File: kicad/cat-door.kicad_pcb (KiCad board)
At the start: 2 copper layers, 25 x 48.6 mm, 18 parts, among them U1 ATtiny84-20PU, U2 L293D, U3 LF50_TO220

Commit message: PCB seems done
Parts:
- removed JPOWER1: Conn_01x02, Connector_PinSocket_2.54mm:PinSocket_1x02_P2.54mm_Vertical
- removed R3: 10k, Resistor_THT:R_Axial_DIN0207_L6.3mm_D2.5mm_P10.16mm_Horizontal
- added G***: LOGO, Cat Door:cat, B.Cu at (85.2, 39.8)
- added J1: Barrel_Jack_Switch, Cat Door:CUI_PJ-044AH, F.Cu at (71.5, 41.9)
- C1, C2, D1, D2, D3, D4, JPENCIL1, R1, R2, R4, R5, U1, U2, U3: moved to B.Cu
- moved R1 37.0 mm to (76.4, 72.4), turned to 180 degrees
- moved U2 36.3 mm to (78.9, 76.0)
- moved D1 32.5 mm to (68.9, 77.1), turned to 0 degrees
- moved R4 31.2 mm to (85.0, 55.4), turned to 90 degrees
- moved D3 28.4 mm to (68.9, 75.0), turned to 0 degrees
- moved R5 27.9 mm to (82.0, 55.4)
- moved U3 24.4 mm to (78.9, 37.6)
- moved JPENCIL1 23.9 mm to (72.7, 61.6), turned to 270 degrees
- moved D4 23.7 mm to (68.9, 66.9), turned to 0 degrees
- moved C2 20.9 mm to (65.2, 39.7), turned to 90 degrees
- moved U1 20.0 mm to (63.6, 47.0), turned to 270 degrees
- moved R2 19.4 mm to (63.7, 67.4)
- moved D2 13.9 mm to (68.9, 64.6), turned to 0 degrees
- moved C1 13.1 mm to (63.1, 44.3), turned to 0 degrees
- moved JCTRL1 7.39 mm to (67.7, 58.1), turned to 90 degrees
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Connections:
- JCTRL1 pad 1: /sw_closed_i -> /sw_open_i
- JCTRL1 pad 2: /sw_open_i -> /sw_closed_i
- JOUTER1 pad 1: /sens_open_i -> Net-(JOUTER1-Pad1)
- JOUTER1 pad 2: /sens_closed_i -> Net-(JOUTER1-Pad2)
- JOUTER1 pad 4: Net-(JOUTER1-Pad4) -> /sens_closed_i
- JOUTER1 pad 5: Net-(JOUTER1-Pad5) -> /sens_open_i
- R4 pad 1: /sw_closed_i -> /sw_open_i
- R5 pad 1: /sw_open_i -> /sw_closed_i
- U1 pad 4: Net-(R3-Pad2) -> +5V
- U2 pad 11: Net-(JOUTER1-Pad4) -> Net-(JOUTER1-Pad1)
- U2 pad 14: Net-(JOUTER1-Pad5) -> Net-(JOUTER1-Pad2)
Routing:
- net +5V: track 54.5 -> 100.6 mm
- net +9V: track 67.8 -> 29.6 mm
- net /sens_open_i: track 27.8 -> 55.5 mm
- net /sens_closed_i: track 21.2 -> 46.3 mm
- net Net-(JOUTER1-Pad1): track 0.00 -> 24.7 mm
- net Net-(JOUTER1-Pad4): track 19.4 -> 0.00 mm
- net Net-(JOUTER1-Pad2): track 0.00 -> 19.1 mm
- net GND: track 92.9 -> 111.8 mm
- net Net-(JOUTER1-Pad5): track 14.9 -> 0.00 mm
- net Net-(JPENCIL1-Pad2): track 19.1 -> 4.39 mm
- net /sw_closed_i: track 25.8 -> 13.5 mm
- net /outer_down_o: track 33.6 -> 45.3 mm
- net /flshgnd: track 21.5 -> 11.7 mm
- net Net-(JPENCIL1-Pad1): track 21.2 -> 12.4 mm
- net /inner_up_o: track 29.3 -> 36.0 mm
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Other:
- board size 25 x 48.6 mm -> 28.9 x 43.1 mm
- board text added: "Mark's Cat Door Rev. 2"

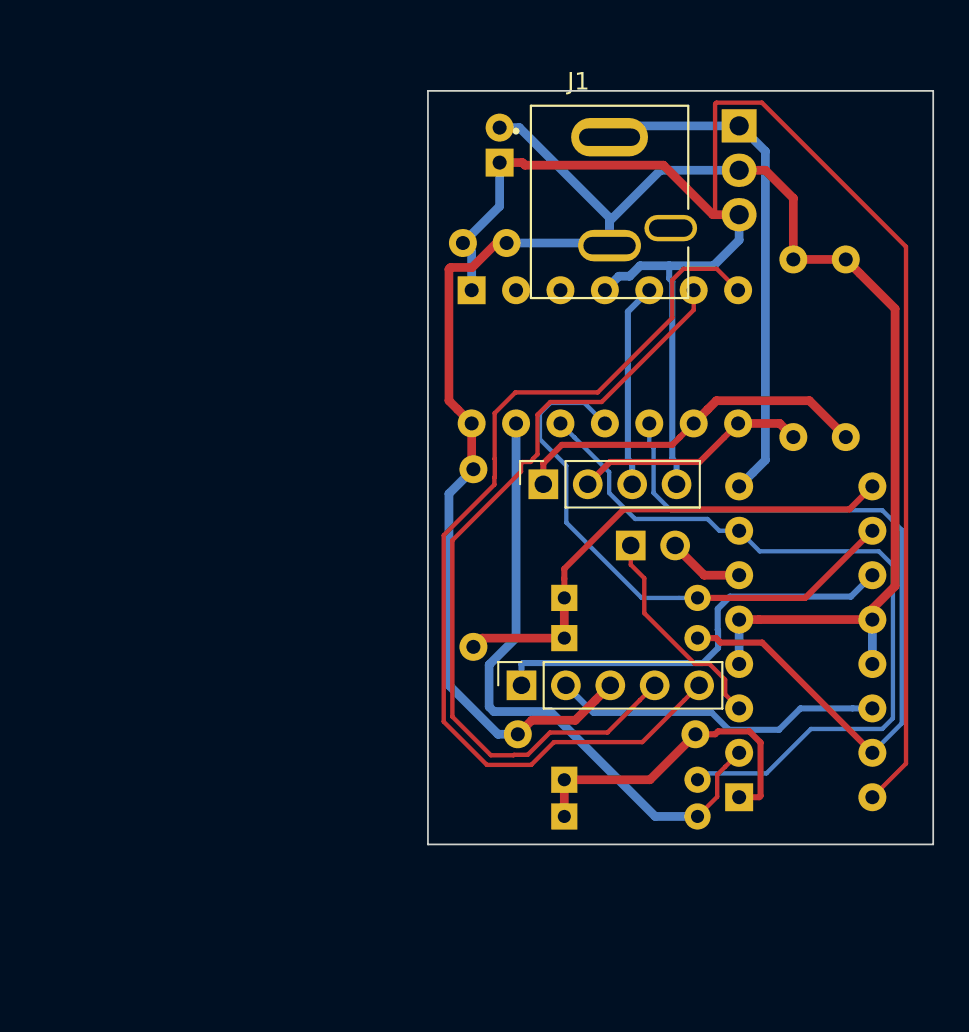
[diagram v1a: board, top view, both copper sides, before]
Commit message: the measurements on the PCb were all wrong. Until now!
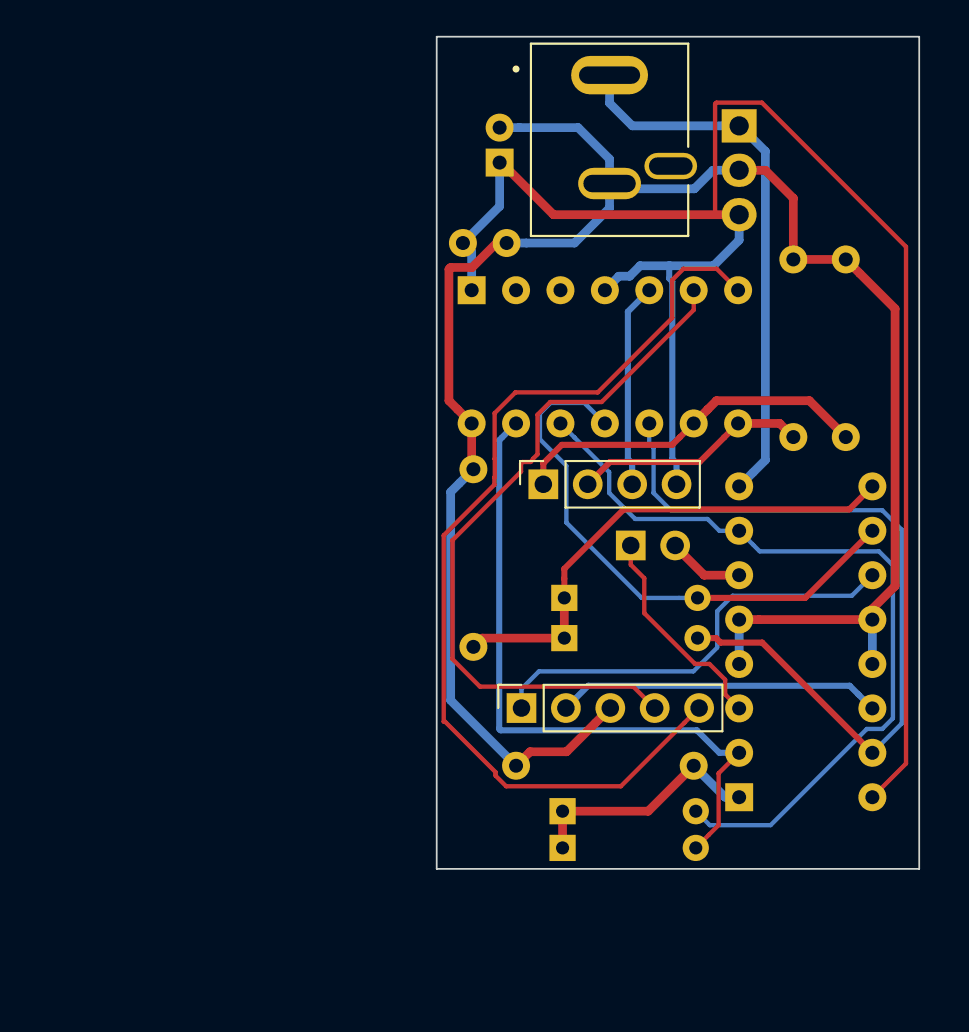
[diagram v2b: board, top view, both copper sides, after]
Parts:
- moved J1 3.55 mm to (71.5, 38.4)
- moved G*** 2.65 mm to (84.7, 37.2)
- moved D1 1.80 mm to (68.8, 78.9)
- moved D3 1.80 mm to (68.8, 76.8)
- moved R1 1.80 mm to (76.3, 74.2)
- moved JOUTER1 1.30 mm to (66.5, 70.9)
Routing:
- net Net-(D1-Pad1): track 19.0 -> 14.0 mm
- net /sens_closed_i: track 46.3 -> 41.5 mm
- net /inner_up_o: track 36.0 -> 38.6 mm
- net +9V: track 29.6 -> 31.4 mm
- net /inner_down_o: track 44.5 -> 46.0 mm
- net /sens_open_i: track 55.5 -> 56.1 mm
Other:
- board size 28.9 x 43.1 mm -> 27.6 x 47.6 mm

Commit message: horizontal and vertical traces separated.
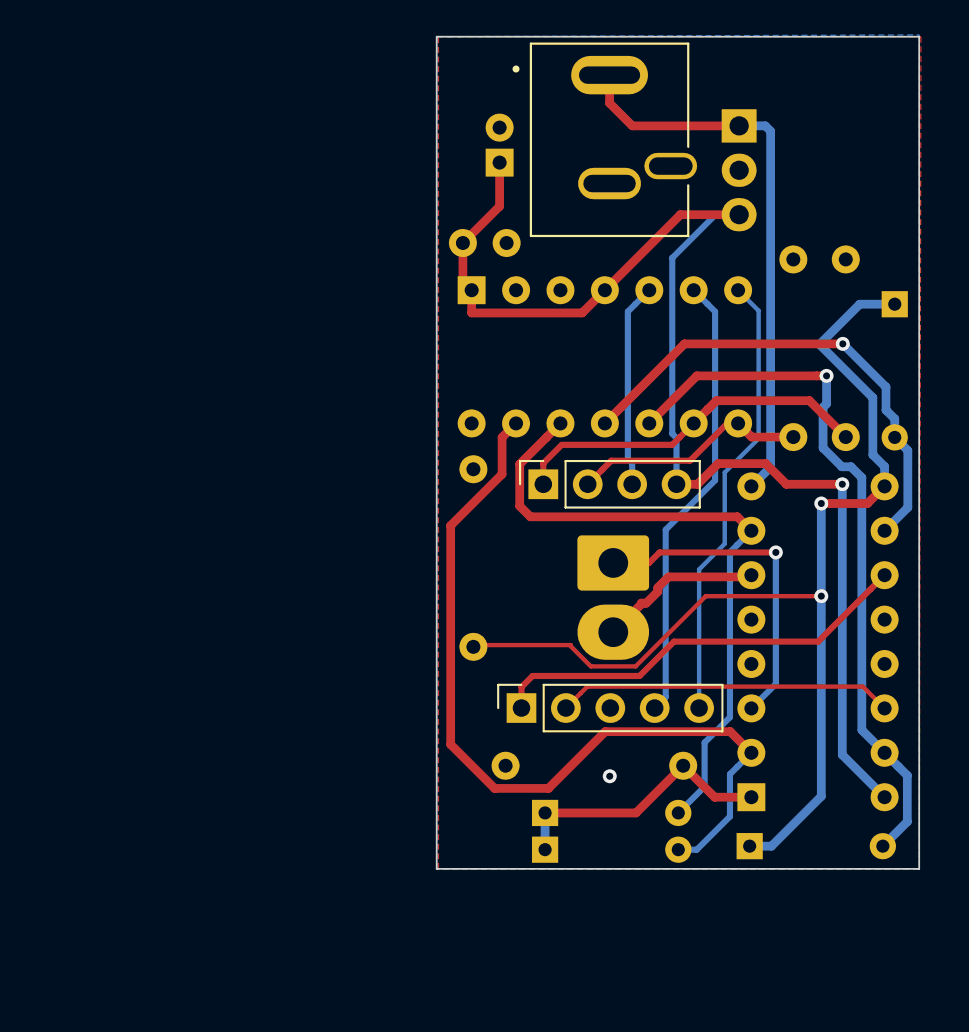
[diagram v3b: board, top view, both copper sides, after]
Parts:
- JPENCIL1: footprint Connector_PinSocket_2.54mm:PinSocket_1x02_P2.54mm_Vertical -> Connector_Molex:Molex_KK-396_A-41791-0002_1x02_P3.96mm_Vertical
- moved D2 25.3 mm to (87.8, 47.8), turned to 270 degrees
- moved D4 15.9 mm to (79.5, 78.8)
- moved JPENCIL1 1.41 mm to (71.7, 62.6)
- moved D3 1.00 mm to (67.8, 76.9)
- moved D1 1.00 mm to (67.8, 79.0)
- moved U2 0.70 mm to (79.6, 76.0)
- moved R1 0.60 mm to (75.7, 74.2)
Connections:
- U1 pad 2: Net-(U1-Pad2) -> GND
- U1 pad 3: Net-(U1-Pad3) -> GND
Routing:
- net GND: track 111.7 -> 0.00 mm, vias 0 -> 1
- net Net-(D2-Pad1): track 28.9 -> 63.1 mm, vias 0 -> 2
- net /sens_open_i: track 56.1 -> 25.8 mm
- net +5V: track 100.6 -> 74.6 mm, vias 0 -> 1
- net /sens_closed_i: track 41.5 -> 25.8 mm
- net /inner_up_o: track 38.6 -> 47.9 mm
- net /inner_down_o: track 46.0 -> 37.4 mm
- net Net-(JPENCIL1-Pad1): track 12.4 -> 19.0 mm, vias 0 -> 1
- net Net-(JPENCIL1-Pad2): track 4.39 -> 9.42 mm
- net /outer_down_o: track 45.3 -> 41.1 mm, vias 0 -> 1
- net /outer_up_o: track 32.2 -> 28.3 mm, vias 0 -> 1
- net Net-(D1-Pad1): track 14.0 -> 15.8 mm
- net +9V: track 31.4 -> 32.3 mm
- net Net-(JOUTER1-Pad2): track 18.6 -> 19.3 mm
- added copper zone on B.Cu, net GND
- added copper zone on F.Cu, net GND

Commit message: lots of stuff. Time to rewrite after hiking!
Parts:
- added C3: .1uF, Capacitor_THT:C_Disc_D3.0mm_W1.6mm_P2.50mm, B.Cu at (65.9, 35.0)
- moved C2 0.57 mm to (65.6, 40.1)
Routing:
- net +9V: track 32.3 -> 38.0 mm
- net +5V: track 74.6 -> 75.1 mm
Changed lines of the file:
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@@
     (thickness 1.6)
     (drawings 5)
-    (tracks 171)
+    (tracks 175)
     (zones 0)
-    (modules 18)
+    (modules 19)
     (nets 20)
   )
@@
     (add_net "Net-(JPENCIL1-Pad1)")
     (add_net "Net-(JPENCIL1-Pad2)")
+  )
+  (module Capacitor_THT:C_Disc_D3.0mm_W1.6mm_P2.50mm (layer B.Cu)
+    (at 65.9 35 180)
+    (descr "C, Disc series, Radial, pin pitch=2.50mm, , diameter*width=3.0*1.6mm^2, Capacitor, http://www.vishay.com/docs/45233/krseries.pdf")
+    (tags "C Disc series Radial pin pitch 2.50mm  diameter 3.0mm width 1.6mm Capacitor")
+    (fp_text reference C3 (at 1.2 1.6) (layer B.SilkS)
+      (effects (font (size 1 1) (thickness 0.15)) (justify mirror))
+    )
+    (fp_text value .1uF (at 1.25 -2.05) (layer B.Fab)
+      (effects (font (size 1 1) (thickness 0.15)) (justify mirror))
+    )
+    (fp_text user %R (at 1.25 0) (layer B.Fab)
+      (effects (font (size 0.6 0.6) (thickness 0.09)) (justify mirror))
+    )
+    (fp_line (start 3.55 1.05) (end -1.05 1.05) (layer B.CrtYd) (width 0.05))
+    (fp_line (start 3.55 -1.05) (end 3.55 1.05) (layer B.CrtYd) (width 0.05))
+    (fp_line (start -1.05 -1.05) (end 3.55 -1.05) (layer B.CrtYd) (width 0.05))
+    (fp_line (start -1.05 1.05) (end -1.05 -1.05) (layer B.CrtYd) (width 0.05))
+    (fp_line (start 0.621 -0.92) (end 1.879 -0.92) (layer B.SilkS) (width 0.12))
+    (fp_line (start 0.621 0.92) (end 1.879 0.92) (layer B.SilkS) (width 0.12))
+    (fp_line (start 2.75 0.8) (end -0.25 0.8) (layer B.Fab) (width 0.1))
+    (fp_line (start 2.75 -0.8) (end 2.75 0.8) (layer B.Fab) (width 0.1))
+    (fp_line (start -0.25 -0.8) (end 2.75 -0.8) (layer B.Fab) (width 0.1))
+    (fp_line (start -0.25 0.8) (end -0.25 -0.8) (layer B.Fab) (width 0.1))
+    (pad 2 thru_hole circle (at 2.5 0 180) (size 1.6 1.6) (drill 0.8) (layers *.Cu *.Mask)
+      (net 11 GND))
+    (pad 1 thru_hole circle (at 0 0 180) (size 1.6 1.6) (drill 0.8) (layers *.Cu *.Mask)
+      (net 16 +9V))
+    (model ${KISYS3DMOD}/Capacitor_THT.3dshapes/C_Disc_D3.0mm_W1.6mm_P2.50mm.wrl
+      (at (xyz 0 0 0))
+      (scale (xyz 1 1 1))
+      (rotate (xyz 0 0 0))
+    )
   )
   (module Connector_Molex:Molex_KK-396_A-41791-0002_1x02_P3.96mm_Vertical (layer B.Cu)
@@
   )
   (module Capacitor_THT:CP_Radial_D5.0mm_P2.00mm (layer B.Cu)
-    (at 65.2 39.7 90)
+    (at 65.6 40.1 90)
     (descr "CP, Radial series, Radial, pin pitch=2.00mm, , diameter=5mm, Electrolytic Capacitor")
     (tags "CP Radial series Radial pin pitch 2.00mm  diameter 5mm Electrolytic Capacitor")
@@
   (segment (start 75.54 42.68) (end 71.22 47) (width 0.5) (layer F.Cu) (net 7))
   (segment (start 78.9 42.68) (end 75.54 42.68) (width 0.5) (layer F.Cu) (net 7))
-  (segment (start 65.2 42.2) (end 63.1 44.3) (width 0.5) (layer F.Cu) (net 7))
-  (segment (start 65.2 39.7) (end 65.2 42.2) (width 0.5) (layer F.Cu) (net 7))
   (segment (start 63.1 46.5) (end 63.6 47) (width 0.5) (layer F.Cu) (net 7))
   (segment (start 63.1 44.3) (end 63.1 46.5) (width 0.5) (layer F.Cu) (net 7))
@@
   (segment (start 81.6 58.1) (end 80.419999 56.919999) (width 0.5) (layer F.Cu) (net 7))
   (segment (start 84.8 58.1) (end 81.6 58.1) (width 0.5) (layer F.Cu) (net 7))
+  (segment (start 63.1 43.16863) (end 63.1 44.3) (width 0.5) (layer F.Cu) (net 7))
+  (segment (start 63.1 41.3) (end 63.1 43.16863) (width 0.5) (layer F.Cu) (net 7))
+  (segment (start 64.3 40.1) (end 63.1 41.3) (width 0.5) (layer F.Cu) (net 7))
+  (segment (start 65.6 40.1) (end 64.3 40.1) (width 0.5) (layer F.Cu) (net 7))
   (segment (start 72.534999 48.225001) (end 72.960001 47.799999) (width 0.35) (layer B.Cu) (net 8))
   (segment (start 72.534999 56.652918) (end 72.534999 48.225001) (width 0.35) (layer B.Cu) (net 8))
@@
   (segment (start 80.7 57.12) (end 80.7 37.9) (width 0.5) (layer B.Cu) (net 16))
   (segment (start 80.7 37.9) (end 80.4 37.6) (width 0.5) (layer B.Cu) (net 16))
+  (segment (start 71.1864 35) (end 71.4883 34.6981) (width 0.5) (layer F.Cu) (net 16))
+  (segment (start 65.9 35) (end 71.1864 35) (width 0.5) (layer F.Cu) (net 16))
   (segment (start 86.420001 64.099999) (end 87.22 63.3) (width 0.35) (layer F.Cu) (net 18))
   (segment (start 83.42 67.1) (end 86.420001 64.099999) (width 0.35) (layer F.Cu) (net 18))
